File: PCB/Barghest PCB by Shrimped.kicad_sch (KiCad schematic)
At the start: 138 parts, among them SW1 RotaryEncoder_Switch, SW2 RotaryEncoder_Switch, U1 RP2040_Pro_Micro

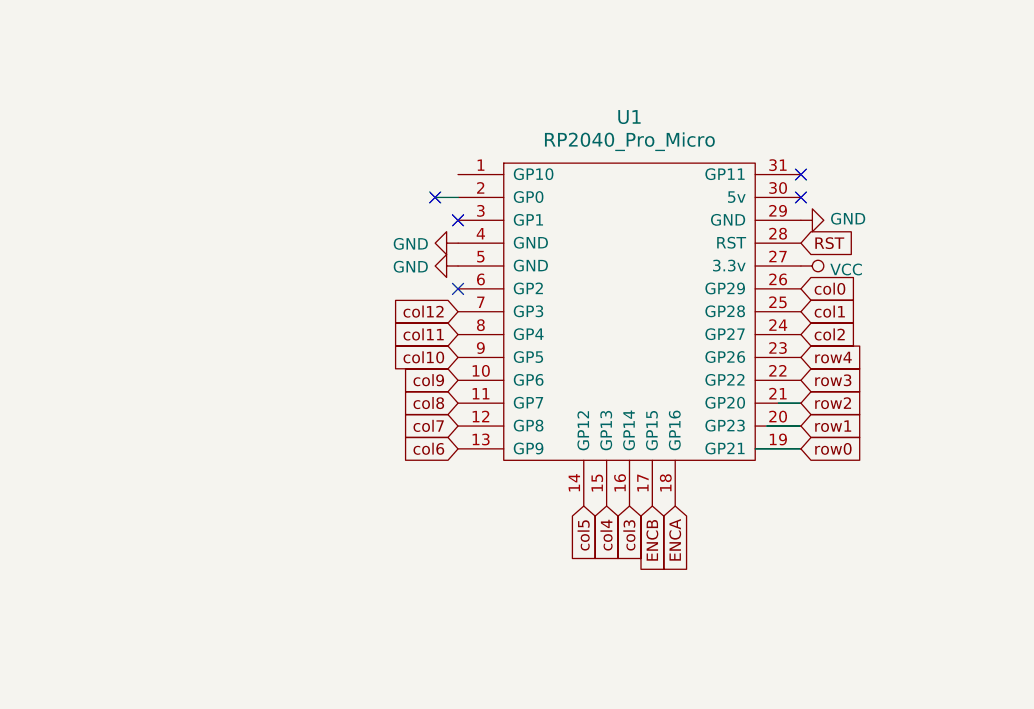
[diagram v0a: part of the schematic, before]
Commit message: Added RGB
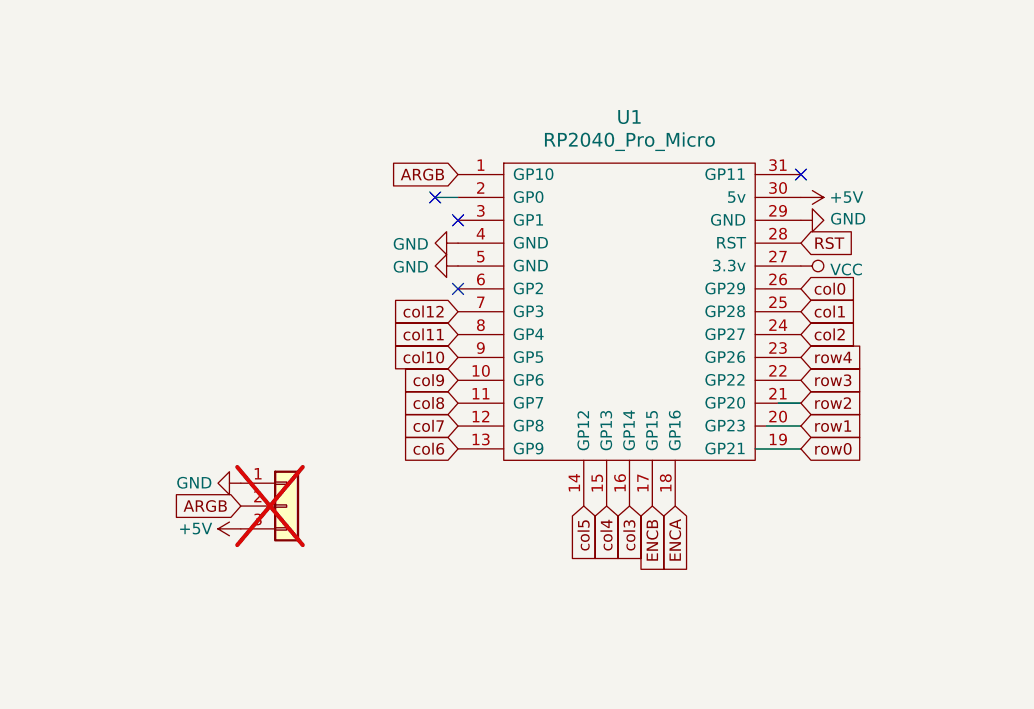
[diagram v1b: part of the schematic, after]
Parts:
- added J1: ARGB, Connector_PinHeader_1.27mm:PinHeader_1x03_P1.27mm_Vertical, symbol Connector_Generic:Conn_01x03
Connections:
- net GND: now also J1.1 (Pin_1)
- net ARGB: now reaches U1.1 (GP10)
- net ARGB: now also J1.2 (Pin_2)
- net +5V: now reaches U1.30 (5v)
- net +5V: now also J1.3 (Pin_3)
- no-connect marks 5 -> 4
